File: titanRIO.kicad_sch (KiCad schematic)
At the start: 19 parts, among them IC1 SLG46110V, J2 Conn_01x10, J3 Conn_01x05, Q2 BSS138, Q3 BSS138, Q4 BSS138, U1 Tang_Nano_20K

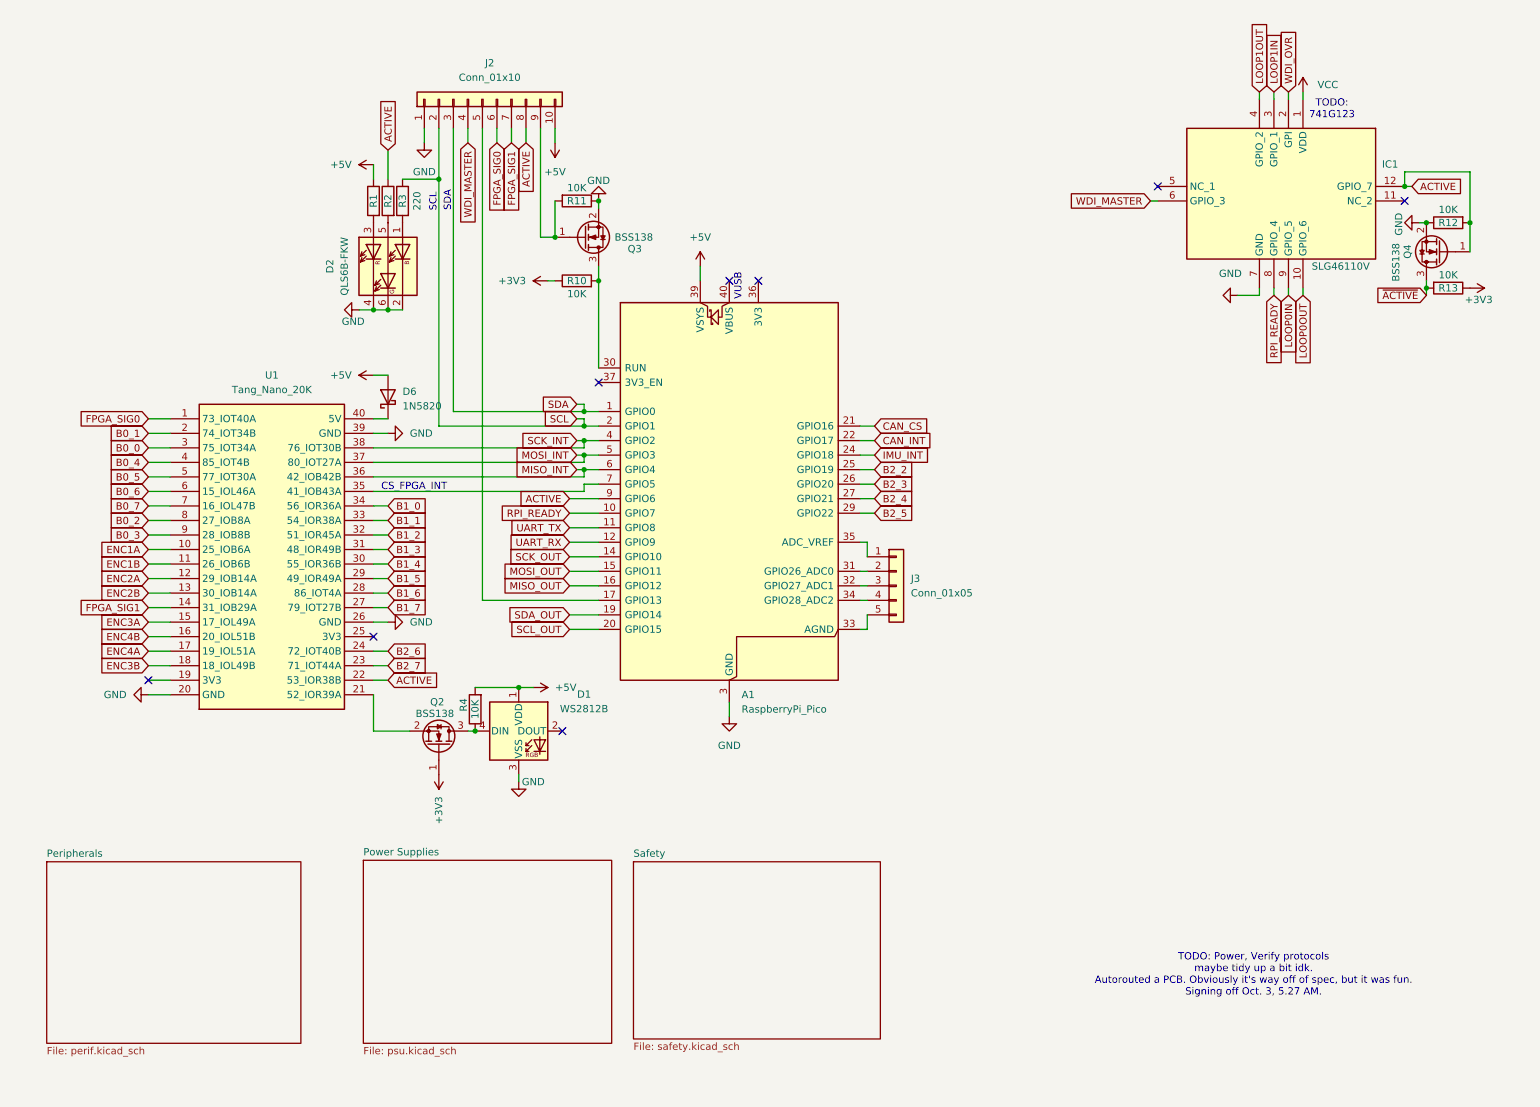
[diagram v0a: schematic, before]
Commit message: Separate safety circuitry, minor schematic changes in main page
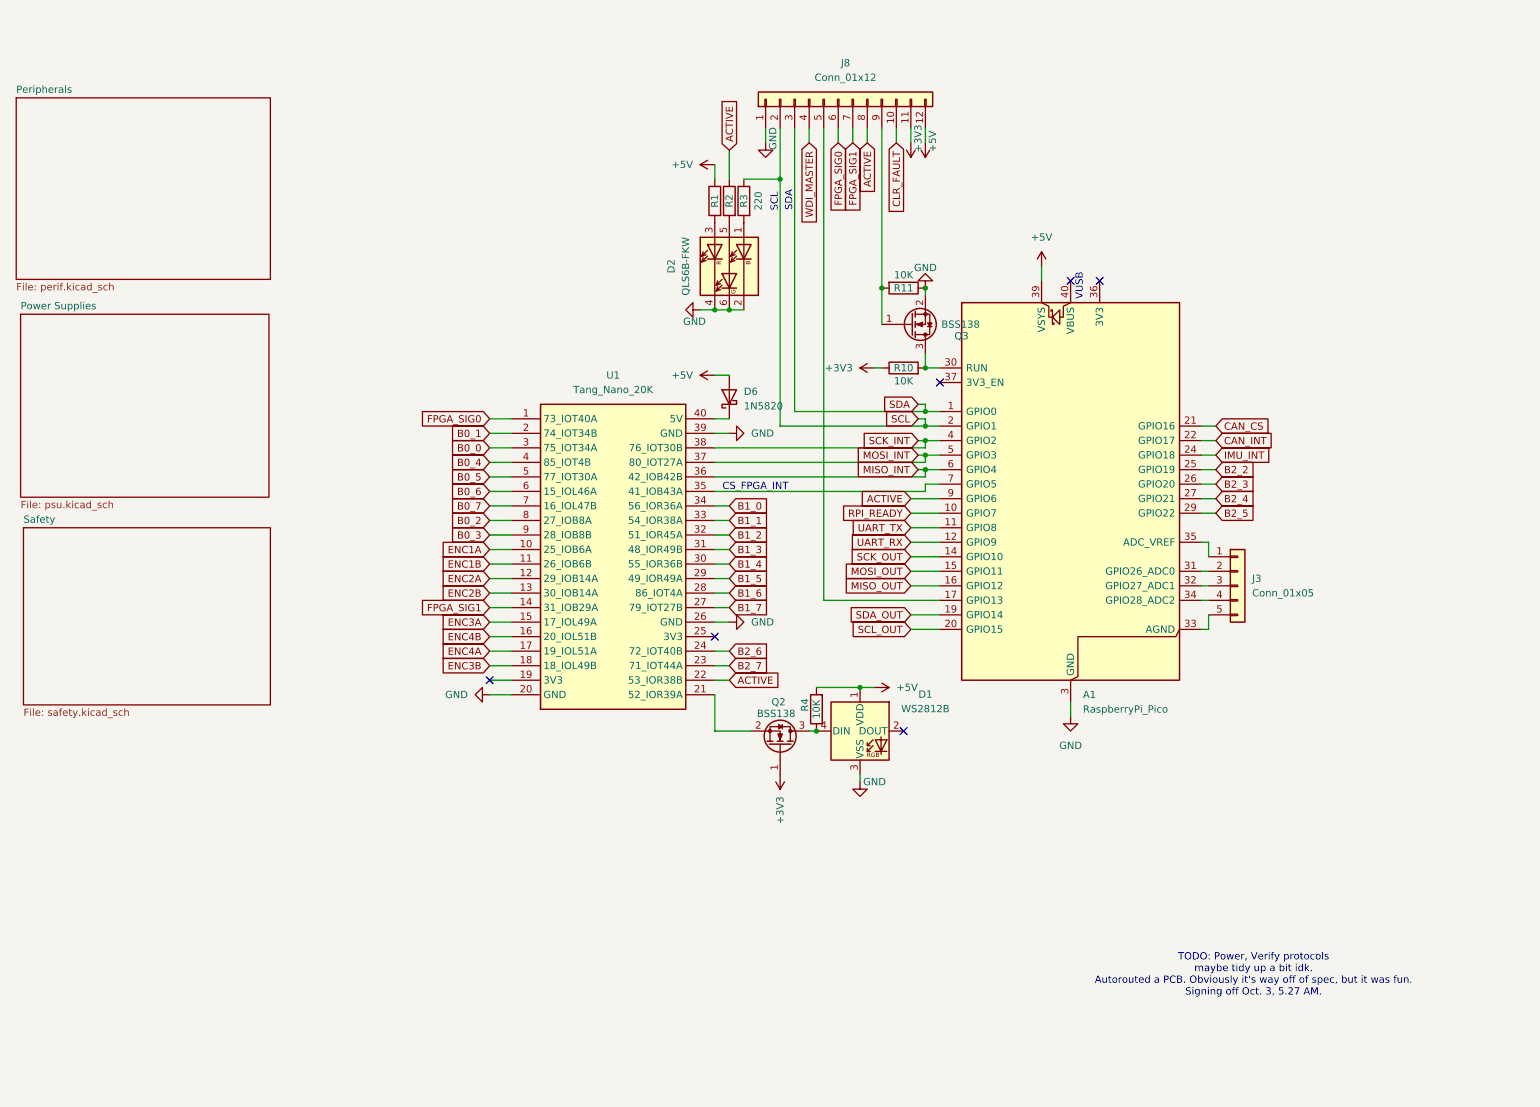
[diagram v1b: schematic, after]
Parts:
- removed IC1: SLG46110V, Samacsys:SLG46110V, symbol Samacsys:SLG46110V
- removed J2: Conn_01x10, Connector_JST:JST_GH_BM10B-GHS-TBT_1x10-1MP_P1.25mm_Vertical, symbol Connector_Generic:Conn_01x10
- removed Q4: BSS138, Package_TO_SOT_SMD:SOT-23, symbol Transistor_FET:BSS138
- removed R12, R13: 10K, Resistor_SMD:R_0805_2012Metric_Pad1.20x1.40mm_HandSolder, symbol Device:R
- added J8: Conn_01x12, Package_DFN_QFN:QFN-20-1EP_5x5mm_P0.65mm_EP3.35x3.35mm, symbol Connector_Generic:Conn_01x12
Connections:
- net +3V3: now also J8.11 (Pin_11)
- net +5V: now also J8.12 (Pin_12)
- net ACTIVE: now also J8.8 (Pin_8)
- net FPGA_SIG0: now also J8.6 (Pin_6)
- net FPGA_SIG1: now also J8.7 (Pin_7)
- net GND: now also J8.1 (Pin_1)
- net SCL: now also J8.2 (Pin_2)
- net SDA: now also J8.3 (Pin_3)
- net WDI_MASTER: now also J8.4 (Pin_4)
- net at Q3.1 (G), R11.2: now also J8.9 (Pin_9)
- net at A1.17 (GPIO13): now also J8.5 (Pin_5)
- new net CLR_FAULT: J8.10 (Pin_10)
- no-connect marks 8 -> 6
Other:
- note removed: "TODO: 741G123"
- moved on the sheet: A1, D1, D2, D6, J3, Q2, Q3, R1, R10, R11, R2, R3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

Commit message: Started on design, minor touch ups on schematic
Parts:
- removed D6: 1N5820, Diode_THT:D_DO-201AD_P15.24mm_Horizontal, symbol Diode:1N5820
- added C1: 105uF, Capacitor_SMD:C_0201_0603Metric_Pad0.64x0.40mm_HandSolder, symbol Device:C
- added C6: 470uF, Capacitor_SMD:CP_Elec_6.3x5.4_Nichicon, symbol Device:C_Polarized_US
- added C7, C8: 180uF, Capacitor_SMD:CP_Elec_6.3x5.4_Nichicon, symbol Device:C_Polarized_US
- added D7, D8, D9: SS32, Diode_SMD:D_SMA, symbol Diode:SS32
- added J1, J11: Screw_Terminal_01x02, TerminalBlock_Phoenix:TerminalBlock_Phoenix_MPT-0,5-2-2.54_1x02_P2.54mm_Horizontal, symbol Connector:Screw_Terminal_01x02
- added JP2: SolderJumper_2_Open, Jumper:SolderJumper-2_P1.3mm_Open_TrianglePad1.0x1.5mm, symbol Jumper:SolderJumper_2_Open
- added L1, L2: 68uH, Inductor_SMD:L_Bourns-SRU8028_8.0x8.0mm, symbol Device:L
- added R14: 0.1, Resistor_SMD:R_2816_7142Metric_Pad3.20x4.45mm_HandSolder, symbol Device:R
- added U12: XL1509-3.3, Package_SO:SOIC-8_3.9x4.9mm_P1.27mm, symbol Regulator_Switching:XL1509-3.3
- added U13: XL1509-5.0, Package_SO:SOIC-8_3.9x4.9mm_P1.27mm, symbol Regulator_Switching:XL1509-5.0
- added U14: INA219AxD, Package_SO:SOIC-8_3.9x4.9mm_P1.27mm, symbol Sensor_Energy:INA219AxD
- J8: footprint Package_DFN_QFN:QFN-20-1EP_5x5mm_P0.65mm_EP3.35x3.35mm -> Connector_JST:JST_GH_BM12B-GHS-TBT_1x12-1MP_P1.25mm_Vertical
- R10, R11, R4: footprint Resistor_SMD:R_0805_2012Metric_Pad1.20x1.40mm_HandSolder -> Resistor_SMD:R_0603_1608Metric_Pad0.98x0.95mm_HandSolder
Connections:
- net +3V3: now also C7.1, L1.2, U12.3 (FB), U14.1 (A1), U14.2 (A0), U14.5 (VS)
- net +5V: now also C8.1, D9.2 (A), L2.2, U13.3 (FB)
- net CLR_FAULT: now also JP2.1 (A); no longer J8.10 (Pin_10)
- net GND: now also C1.2, C6.2, C7.2, C8.2, D7.2 (A), D8.2 (A), J1.1 (Pin_1), J11.1 (Pin_1), U12.4 (~{EN}), U12.5 (GND), U12.6 (GND), U12.7 (GND), U12.8 (GND), U13.4 (~{EN}), U13.5 (GND), U13.6 (GND), U13.7 (GND), U13.8 (GND), U14.6 (GND)
- net SCL_OUT: now also U14.4 (SCL)
- net SDA_OUT: now also U14.3 (SDA)
- net at U1.40 (5V): now also D9.1 (K)
- new net: C1.1, C6.1, J11.2 (Pin_2), R14.2, U12.1 (VIN), U13.1 (VIN), U14.7 (IN-)
- new net: J8.10 (Pin_10), JP2.2 (B)
- new net: D8.1 (K), L2.1, U13.2 (OUT)
- new net: J1.2 (Pin_2), R14.1, U14.8 (IN+)
- new net: D7.1 (K), L1.1, U12.2 (OUT)
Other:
- removed sheet Power Supplies
- note added: "0x45"
- note added: "R14 expects <4A, should need to handle 2W. Pick HPWR 2512 resistor."
- moved on the sheet: A1, D1, D2, J3, J8, Q2, Q3, R1, R10, R11, R2, R3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

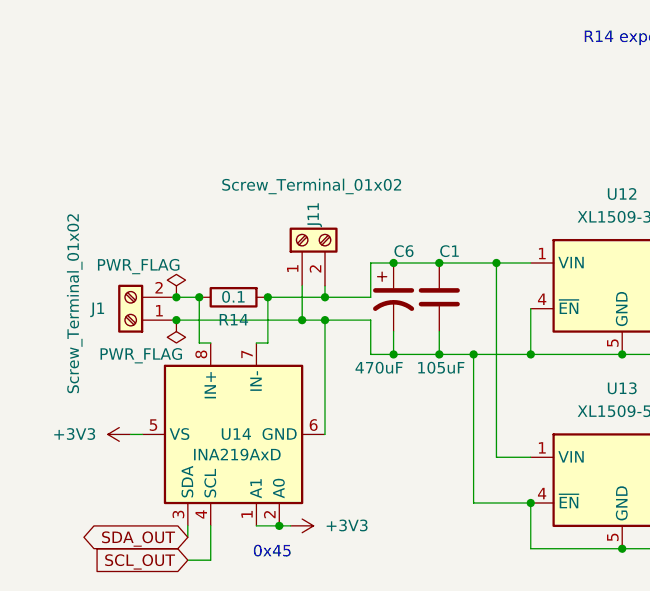
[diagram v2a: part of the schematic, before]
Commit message: Fixed up minor mistakes and reversed terminals in psu. DO THE COPPER POUR, DAMNIT
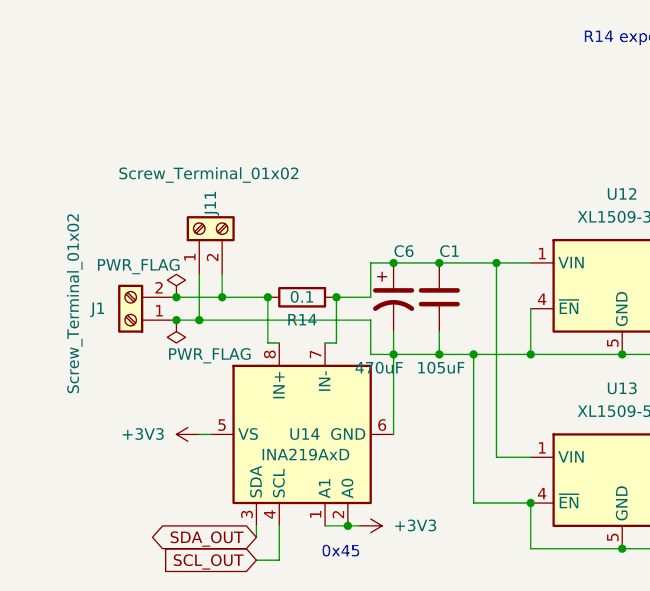
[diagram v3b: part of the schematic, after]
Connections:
- net at C1.1, C6.1, R14.2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: no longer J11.2 (Pin_2)
- net at J1.2 (Pin_2), R14.1, U14.8 (IN+): now also J11.2 (Pin_2)
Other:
- moved on the sheet: J11, R14, U14

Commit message: Implementing just so much stuff. RP2350B on board, new sensors, PSU magic, buncha stuff
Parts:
- removed C1: 105uF, Capacitor_SMD:C_0201_0603Metric_Pad0.64x0.40mm_HandSolder, symbol Device:C
- removed C6: 470uF, Capacitor_SMD:CP_Elec_6.3x5.4_Nichicon, symbol Device:C_Polarized_US
- removed C7, C8: 180uF, Capacitor_SMD:CP_Elec_6.3x5.4_Nichicon, symbol Device:C_Polarized_US
- removed D2: QLS6B-FKW, LED_SMD:LED_Cree-PLCC6_4.7x1.5mm, symbol LED:QLS6B-FKW
- removed D7, D8: SS32, Diode_SMD:D_SMA, symbol Diode:SS32
- removed J1, J11: Screw_Terminal_01x02, TerminalBlock_Phoenix:TerminalBlock_Phoenix_MPT-0,5-2-2.54_1x02_P2.54mm_Horizontal, symbol Connector:Screw_Terminal_01x02
- removed L1, L2: 68uH, Inductor_SMD:L_Bourns-SRU8028_8.0x8.0mm, symbol Device:L
- removed R14: 0.1, Resistor_SMD:R_2816_7142Metric_Pad3.20x4.45mm_HandSolder, symbol Device:R
- removed U12: XL1509-3.3, Package_SO:SOIC-8_3.9x4.9mm_P1.27mm, symbol Regulator_Switching:XL1509-3.3
- removed U13: XL1509-5.0, Package_SO:SOIC-8_3.9x4.9mm_P1.27mm, symbol Regulator_Switching:XL1509-5.0
- removed U14: INA219AxD, Package_SO:SOIC-8_3.9x4.9mm_P1.27mm, symbol Sensor_Energy:INA219AxD
- added D10, D11, D6: LED, LED_SMD:LED_1206_3216Metric, symbol Device:LED
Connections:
- net GND: now also D10.1 (K), D11.1 (K), D6.1 (K)
- net at R3.2: now also D10.2 (A)
- net at R1.2: now also D11.2 (A)
- net at R2.2: now also D6.2 (A)
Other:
- added sheet Power Supply (psu.kicad_sch)
- added sheet pico (pico.kicad_sch)
- note added: "ask abt res div from mode v to rpi vusb tps pr1 res div footprints hooking up the reverse voltage circuitry idk look over a bunch of stuff commit to the pico and finish at least that design COPPER POURS N SHI"
- note removed: "0x45"
- note removed: "R14 expects <4A, should need to handle 2W. Pick HPWR 2512 resistor."

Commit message: Switched back to 2350A, rewired FPGA pins, maybe added some stuff? Idk.
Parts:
- removed A1: RaspberryPi_Pico, Module:RaspberryPi_Pico_Common_Unspecified, symbol MCU_Module:RaspberryPi_Pico
- removed D1: WS2812B, LED_SMD:LED_WS2812B_PLCC4_5.0x5.0mm_P3.2mm, symbol LED:WS2812B
- removed D10, D11, D6: LED, LED_SMD:LED_1206_3216Metric, symbol Device:LED
- removed D9: SS32, Diode_SMD:D_SMA, symbol Diode:SS32
- removed J3: Conn_01x05, Connector_JST:JST_GH_BM05B-GHS-TBT_1x05-1MP_P1.25mm_Vertical, symbol Connector_Generic:Conn_01x05
- removed J8: Conn_01x12, Connector_JST:JST_GH_BM12B-GHS-TBT_1x12-1MP_P1.25mm_Vertical, symbol Connector_Generic:Conn_01x12
- removed JP2: SolderJumper_2_Open, Jumper:SolderJumper-2_P1.3mm_Open_TrianglePad1.0x1.5mm, symbol Jumper:SolderJumper_2_Open
- removed Q2, Q3: BSS138, Package_TO_SOT_SMD:SOT-23, symbol Transistor_FET:BSS138
- removed R1, R2, R3: 220, Resistor_SMD:R_0805_2012Metric_Pad1.20x1.40mm_HandSolder, symbol Device:R
- removed R10, R11, R4: 10K, Resistor_SMD:R_0603_1608Metric_Pad0.98x0.95mm_HandSolder, symbol Device:R
- removed U1: Tang_Nano_20K, 0my_project:DIP-40_TangNano20K, symbol 0my_project:Tang_Nano_20K
- added C26, C27, C30, C31, C32, C50, C56, C57, C58, C59, C60, C61, C62: 100nF, Capacitor_SMD:C_0402_1005Metric, symbol Device:C
- added C29: 10u, Capacitor_SMD:C_0402_1005Metric, symbol Device:C
- added C33: 470uF, Capacitor_SMD:CP_Elec_6.3x5.4_Nichicon, symbol Device:C_Polarized_US
- added C37: 10uF, Capacitor_SMD:C_0805_2012Metric, symbol Device:C
- added C38, C41, C43, C44: 22uF, Capacitor_SMD:C_0603_1608Metric, symbol Device:C
- added C40, C42: 100nF, Capacitor_SMD:C_0603_1608Metric, symbol Device:C
- added C51, C54: 4.7uF, Capacitor_SMD:C_0402_1005Metric, symbol Device:C
- added C52, C53: 15p, Capacitor_SMD:C_0402_1005Metric, symbol Device:C
- added C55: 4.7u, Capacitor_SMD:C_0402_1005Metric, symbol Device:C
- added D15, D16, D9: LED, LED_SMD:LED_1206_3216Metric, symbol Device:LED
- added D5: WS2812B, LED_SMD:LED_WS2812B_PLCC4_5.0x5.0mm_P3.2mm, symbol LED:WS2812B
- added D7: SMAJ18A, Diode_SMD:D_SMA, symbol Diode:SMAJ18A
- added F1: 2920L600/24SL, Fuse:Fuse_2920_7451Metric, symbol Device:Polyfuse
- added J16: Conn_01x03_MountingPin, Connector_JST:JST_GH_SM03B-GHS-TB_1x03-1MP_P1.25mm_Horizontal, symbol Connector_Generic_MountingPin:Conn_01x03_MountingPin
- added J17: USB_C_Receptacle_USB2.0_16P, Connector_USB:USB_C_Receptacle_GCT_USB4105-xx-A_16P_TopMnt_Horizontal, symbol Connector:USB_C_Receptacle_USB2.0_16P
- added J23, J3: Screw_Terminal_01x02, TerminalBlock_Phoenix:TerminalBlock_Phoenix_MPT-0,5-2-2.54_1x02_P2.54mm_Horizontal, symbol Connector:Screw_Terminal_01x02
- added J24: Conn_01x12, Connector_JST:JST_GH_BM12B-GHS-TBT_1x12-1MP_P1.25mm_Vertical, symbol Connector_Generic:Conn_01x12
- added J26: Conn_01x08, Connector_JST:JST_GH_BM08B-GHS-TBT_1x08-1MP_P1.25mm_Vertical, symbol Connector_Generic:Conn_01x08
- added JP6: SolderJumper_2_Open, Jumper:SolderJumper-2_P1.3mm_Open_TrianglePad1.0x1.5mm, symbol Jumper:SolderJumper_2_Open
- added L2, L5: 4.7uH, Inductor_SMD:L_0805_2012Metric, symbol Device:L
- added L6: 3.3uH, Capacitor_SMD:C_0805_2012Metric_Pad1.18x1.45mm_HandSolder, symbol Device:L
- added Q10, Q11: BSS138, Package_TO_SOT_SMD:SOT-23, symbol Transistor_FET:BSS138
- added Q2: DMP3099L, Package_TO_SOT_SMD:SOT-23, symbol Transistor_FET:DMP3099L
- added R13, R22, R7: 220, Resistor_SMD:R_0805_2012Metric_Pad1.20x1.40mm_HandSolder, symbol Device:R
- added R23, R24: 27, Resistor_SMD:R_0402_1005Metric, symbol Device:R
- added R28, R55: 1k, Resistor_SMD:R_0402_1005Metric, symbol Device:R
- added R34: 100K, Resistor_SMD:R_0402_1005Metric, symbol Device:R
- added R37: 0.1, Resistor_SMD:R_2816_7142Metric_Pad3.20x4.45mm_HandSolder, symbol Device:R
- added R38: 33K, Resistor_SMD:R_0402_1005Metric, symbol Device:R
- added R39: 10K, Resistor_SMD:R_0402_1005Metric, symbol Device:R
- added R51, R52, R59: 10K, Resistor_SMD:R_0603_1608Metric_Pad0.98x0.95mm_HandSolder, symbol Device:R
- added R53, R54: 100R, Resistor_SMD:R_0402_1005Metric_Pad0.72x0.64mm_HandSolder, symbol Device:R
- added R56: 33, Resistor_SMD:R_0402_1005Metric, symbol Device:R
- added R57, R58: 5.1K, Resistor_SMD:R_0402_1005Metric, symbol Device:R
- added SW6: SW_Push, Button_Switch_SMD:SW_Push_1P1T_NO_CK_KMR2, symbol Switch:SW_Push
- added U14: RP2350A-QFN60, Package_DFN_QFN:QFN-60-1EP_7x7mm_P0.4mm_EP3.4x3.4mm, symbol RP2350x:RP2350A-QFN60
- added U21: W25Q128JVS, Package_SO:SOIC-8_5.3x5.3mm_P1.27mm, symbol Memory_Flash:W25Q128JVS
- added U23: INA219AxD, Package_SO:SOIC-8_3.9x4.9mm_P1.27mm, symbol Sensor_Energy:INA219AxD
- added U25: AP63203WU, Package_TO_SOT_SMD:TSOT-23-6, symbol Regulator_Switching:AP63203WU
- added U26: AP63205WU, Package_TO_SOT_SMD:TSOT-23-6, symbol Regulator_Switching:AP63205WU
- added U27: TPS2116DRL, Package_TO_SOT_SMD:SOT-583-8, symbol Power_Management:TPS2116DRL
- added U29: MB85RS256B, Package_SO:SO-8_3.9x4.9mm_P1.27mm, symbol Memory_NVRAM:MB85RS256B
- added Y5: 12MHz, Oscillator:Oscillator_SMD_Abracon_ASE-4Pin_3.2x2.5mm, symbol Device:Crystal_GND24
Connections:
- net +3V3: now also C26.1, C27.1, C29.1, C30.1, C31.1, C32.1, C38.1, C41.1, C50.2, C51.1, C56.1, C57.1, C58.1, C59.1, J24.11 (Pin_11), J26.7 (Pin_7), L5.2, Q11.1 (G), R52.1, R56.1, U14.1 (IOVDD), U14.11 (IOVDD), U14.20 (IOVDD), U14.30 (IOVDD), U14.38 (IOVDD), U14.44 (ADC_AVDD), U14.45 (IOVDD), U14.49 (VREG_VIN), U14.53 (USB_OTP_VDD), U14.54 (QSPI_IOVDD), U21.8 (VCC), U23.2 (A0), U23.5 (VS), U25.1 (FB), U29.3 (~{WP}), U29.7 (~{HOLD}), U29.8 (VDD)
- net +5V: now also D5.1 (VDD), J24.12 (Pin_12), R59.2, R7.1, U25.2 (EN), U25.3 (IN), U27.2 (VOUT), U27.7 (VOUT)
- net ACTIVE: now also J24.8 (Pin_8), R13.1, U14.9 (GPIO6)
- net CAN_CS: now also U14.32 (GPIO20)
- net CAN_INT: now also U14.33 (GPIO21)
- net CLR_FAULT: now also JP6.1 (A)
- net FPGA_SIG0: now also J24.6 (Pin_6)
- net FPGA_SIG1: now also J24.7 (Pin_7)
- net GND: now also C26.2, C27.2, C29.2, C30.2, C31.2, C32.2, C33.2, C37.2, C38.2, C41.2, C43.2, C44.2, C50.1, C51.2, C52.1, C53.1, C54.2, C55.1, C56.2, C57.2, C58.2, C59.2, C60.2, C61.2, C62.2, D15.1 (K), D16.1 (K), D5.3 (VSS), D9.1 (K), J16.2 (Pin_2), J16.MP (MountPin), J17.A1 (GND), J17.A12 (GND), J17.B1 (GND), J17.B12 (GND), J17.SH (SHIELD), J23.1 (Pin_1), J24.1 (Pin_1), J26.8 (Pin_8), J3.1 (Pin_1), Q10.2 (S), R34.2, R39.1, R51.1, R57.2, R58.1, SW6.1, U14.47 (VREG_PGND), U14.61 (GND), U21.4 (GND), U23.6 (GND), U25.4 (GND), U26.4 (GND), U27.1 (GND), U29.4 (GND), Y5.2 (G), Y5.4 (G)
- net IMU_INT: now also U14.29 (GPIO18)
- net MISO_INT: now also U14.7 (GPIO4), U29.2 (SO)
- net MISO_OUT: now also U14.16 (GPIO12)
- net MOSI_INT: now also U14.5 (GPIO3), U29.5 (SI)
- net MOSI_OUT: now also U14.15 (GPIO11)
- net RPI_READY: now also U14.10 (GPIO7)
- net SCK_INT: now also U14.4 (GPIO2), U29.6 (SCK)
- net SCK_OUT: now also U14.14 (GPIO10)
- net SCL: now also J24.2 (Pin_2), R22.1, U14.3 (GPIO1)
- net SCL_OUT: now also U14.19 (GPIO15), U23.4 (SCL)
- net SDA: now also J24.3 (Pin_3), U14.2 (GPIO0)
- net SDA_OUT: now also U14.18 (GPIO14), U23.1 (A1), U23.3 (SDA)
- net UART_RX: now also U14.13 (GPIO9)
- net UART_TX: now also U14.12 (GPIO8)
- net WDI_MASTER: now also J24.4 (Pin_4)
- new net: C33.1, C37.1, R37.2, U23.7 (IN-), U26.2 (EN), U26.3 (IN)
- new net: C42.2, L2.1, U26.5 (SW)
- new net: R23.1, U14.52 (USB_DP)
- new net: J17.A6 (D+), J17.B6 (D+), R23.2
- new net: D7.1 (A1), Q2.2 (S), R37.1, U23.8 (IN+)
- new net: J16.1 (Pin_1), R53.1
- new net: R53.2, U14.24 (SWCLK)
- new net: F1.1, J3.2 (Pin_2)
- new net: F1.2, J23.2 (Pin_2), Q2.3 (D)
- new net: C40.2, L5.1, U25.5 (SW)
- new net: C40.1, U25.6 (BST)
- new net: D9.2 (A), R13.2
- new net: D16.2 (A), R22.2
- new net: J17.A7 (D-), J17.B7 (D-), R24.1
- new net: R24.2, U14.51 (USB_DM)
- new net: C52.2, U14.21 (XIN), Y5.1
- new net: C53.2, R55.1, Y5.3
- new net: Q10.3 (D), R52.2, U14.26 (RUN)
- new net: R38.1, R39.2, U27.4 (PR1)
- new net: U14.34 (GPIO22), U29.1 (~{CS})
- new net: L6.2, U14.48 (VREG_LX)
- new net: D7.2 (A2), Q2.1 (G), R34.1
- new net: R55.2, U14.22 (XOUT)
- new net: R54.1, U14.25 (SWDIO)
- new net: Q11.2 (S), U14.35 (GPIO23)
- new net: J26.1 (Pin_1), U14.36 (GPIO24)
- new net: J26.2 (Pin_2), U14.37 (GPIO25)
- new net: J26.3 (Pin_3), U14.40 (GPIO26_ADC0)
- new net: J26.4 (Pin_4), U14.41 (GPIO27_ADC1)
- new net: J26.5 (Pin_5), U14.42 (GPIO28_ADC2)
- new net: J26.6 (Pin_6), U14.43 (GPIO29_ADC3)
- new net: C55.2, R56.2, U14.46 (VREG_AVDD)
- new net: U14.55 (QSPI_SD3), U21.7 (~{HOLD}/~{RESET}/IO_{3})
- new net: U14.56 (QSPI_SCLK), U21.6 (CLK)
- new net: U14.57 (QSPI_SD0), U21.5 (DI/IO_{0})
- new net: U14.58 (QSPI_SD2), U21.3 (~{WP}/IO_{2})
- new net: U14.59 (QSPI_SD1), U21.2 (DO/IO_{1})
- new net: R28.2, U14.60 (QSPI_SS), U21.1 (~{CS})
- new net: R28.1, SW6.2
- new net: D15.2 (A), R7.2
- new net: D5.4 (DIN), Q11.3 (D), R59.1
- new net: J24.10 (Pin_10), JP6.2 (B)
- new net: C42.1, U26.6 (BST)
- new net: J16.3 (Pin_3), R54.2
- new net: J17.A5 (CC1), R58.2
- new net: J17.B5 (CC2), R57.1
- new net +1V1: C54.1, C60.1, C61.1, C62.1, L6.1, U14.23 (DVDD), U14.39 (DVDD), U14.50 (VREG_FB), U14.6 (DVDD)
- new net 5V_REG: C43.1, C44.1, L2.2, R38.2, U26.1 (FB), U27.3 (VIN1), U27.5 (MODE)
- new net FPGA_CS: U14.8 (GPIO5)
- new net MASTER_INT: J24.5 (Pin_5), U14.17 (GPIO13)
- new net MODE_V: U27.8 (ST)
- new net PPS: U14.31 (GPIO19)
- new net RUN: J24.9 (Pin_9), Q10.1 (G), R51.2
- new net RX_INT: U14.28 (GPIO17)
- new net TX_INT: U14.27 (GPIO16)
- new net VUSB: J17.A4 (VBUS), J17.A9 (VBUS), J17.B4 (VBUS), J17.B9 (VBUS), U27.6 (VIN2)
- no-connect marks 6 -> 3
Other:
- removed sheet Power Supply
- removed sheet pico
- note added: "0x49"
- note added: "Power Management"
- note added: "R14 expects <4A, should need to handle 2W. Pick HPWR 2512 resistor."
- note added: "UART0"
- note added: "UART1"
- note added: "We have so much free gpio now LMAO (counting the B2_x leftovers) 3 pins off the FPGA 10 pins off the Pico"
- note removed: "CS_FPGA_INT"
- note removed: "SCL"
- note removed: "SDA"
- note removed: "TODO: Power, Verify protocols maybe tidy up a bit idk. Autorouted a PCB. Obviously it's way off of spec, but it was fun. Signing off Oct. 3, 5.27 AM."
- note removed: "VUSB"
- note removed: "ask abt res div from mode v to rpi vusb tps pr1 res div footprints hooking up the reverse voltage circuitry idk look over a bunch of stuff commit to the pico and finish at least that design COPPER POURS N SHI"

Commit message: PCB Design initialized. And mostly done tbf
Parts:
- removed C33: 470uF, Capacitor_SMD:CP_Elec_6.3x5.4_Nichicon, symbol Device:C_Polarized_US
- removed C37: 10uF, Capacitor_SMD:C_0805_2012Metric, symbol Device:C
- removed J16: Conn_01x03_MountingPin, Connector_JST:JST_GH_SM03B-GHS-TB_1x03-1MP_P1.25mm_Horizontal, symbol Connector_Generic_MountingPin:Conn_01x03_MountingPin
- removed L6: 3.3uH, Capacitor_SMD:C_0805_2012Metric_Pad1.18x1.45mm_HandSolder, symbol Device:L
- added C34: 470uF, Capacitor_SMD:CP_Elec_6.3x5.4_Nichicon, symbol Device:C_Polarized_US
- added C39: 10uF, Capacitor_SMD:C_0805_2012Metric, symbol Device:C
- added J2: Conn_01x03, Connector_JST:JST_XH_B3B-XH-AM_1x03_P2.50mm_Vertical, symbol Connector_Generic:Conn_01x03
- added L1: 3.3uH, Inductor_SMD:L_0805_2012Metric_Pad1.05x1.20mm_HandSolder, symbol Device:L_Polarized
- C26, C27, C30, C31, C32, C56, C57, C58, C59, C60, C61, C62: footprint Capacitor_SMD:C_0402_1005Metric -> Capacitor_SMD:C_0201_0603Metric
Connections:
- net +1V1: now also L1.1
- net +3V3: now also J26.2 (Pin_2); no longer J26.7 (Pin_7)
- net GND: now also J26.1 (Pin_1), C34.2, C39.2, J2.2 (Pin_2); no longer J26.8 (Pin_8)
- net RPI_READY: now also U14.34 (GPIO22); no longer U14.10 (GPIO7)
- net at D7.1 (A1), Q2.2 (S), R37.1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: now also C34.1, C39.1
- net at R53.1: now also J2.3 (Pin_3)
- net at F1.1, J3.2 (Pin_2): now also J23.2 (Pin_2)
- net at F1.2, Q2.3 (D): no longer J23.2 (Pin_2)
- net at U29.1 (~{CS}): now also U14.10 (GPIO7); no longer U14.34 (GPIO22)
- net at U14.48 (VREG_LX): now also L1.2
- net at U14.36 (GPIO24): now also J26.8 (Pin_8); no longer J26.1 (Pin_1)
- net at U14.37 (GPIO25): now also J26.7 (Pin_7); no longer J26.2 (Pin_2)
- net at U14.40 (GPIO26_ADC0): now also J26.6 (Pin_6); no longer J26.3 (Pin_3)
- net at U14.41 (GPIO27_ADC1): now also J26.5 (Pin_5); no longer J26.4 (Pin_4)
- net at U14.42 (GPIO28_ADC2): now also J26.4 (Pin_4); no longer J26.5 (Pin_5)
- net at U14.43 (GPIO29_ADC3): now also J26.3 (Pin_3); no longer J26.6 (Pin_6)
- net at R54.2: now also J2.1 (Pin_1)
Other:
- moved on the sheet: C42, C43, C44, D7, F1, J23, J26, J3, L2, Q2, R34, U26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

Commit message: PSU redesign, or so I tried
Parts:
- C34: footprint Capacitor_SMD:CP_Elec_6.3x5.4_Nichicon -> Capacitor_SMD:CP_Elec_8x10
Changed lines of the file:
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@@
 			)
 		)
-		(property "Footprint" "Capacitor_SMD:CP_Elec_6.3x5.4_Nichicon"
+		(property "Footprint" "Capacitor_SMD:CP_Elec_8x10"
 			(at 69.85 158.75 0)
 			(hide yes)
